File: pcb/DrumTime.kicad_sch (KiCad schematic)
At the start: 5 parts, among them U1 ESP32-S3-WROOM-1-N8

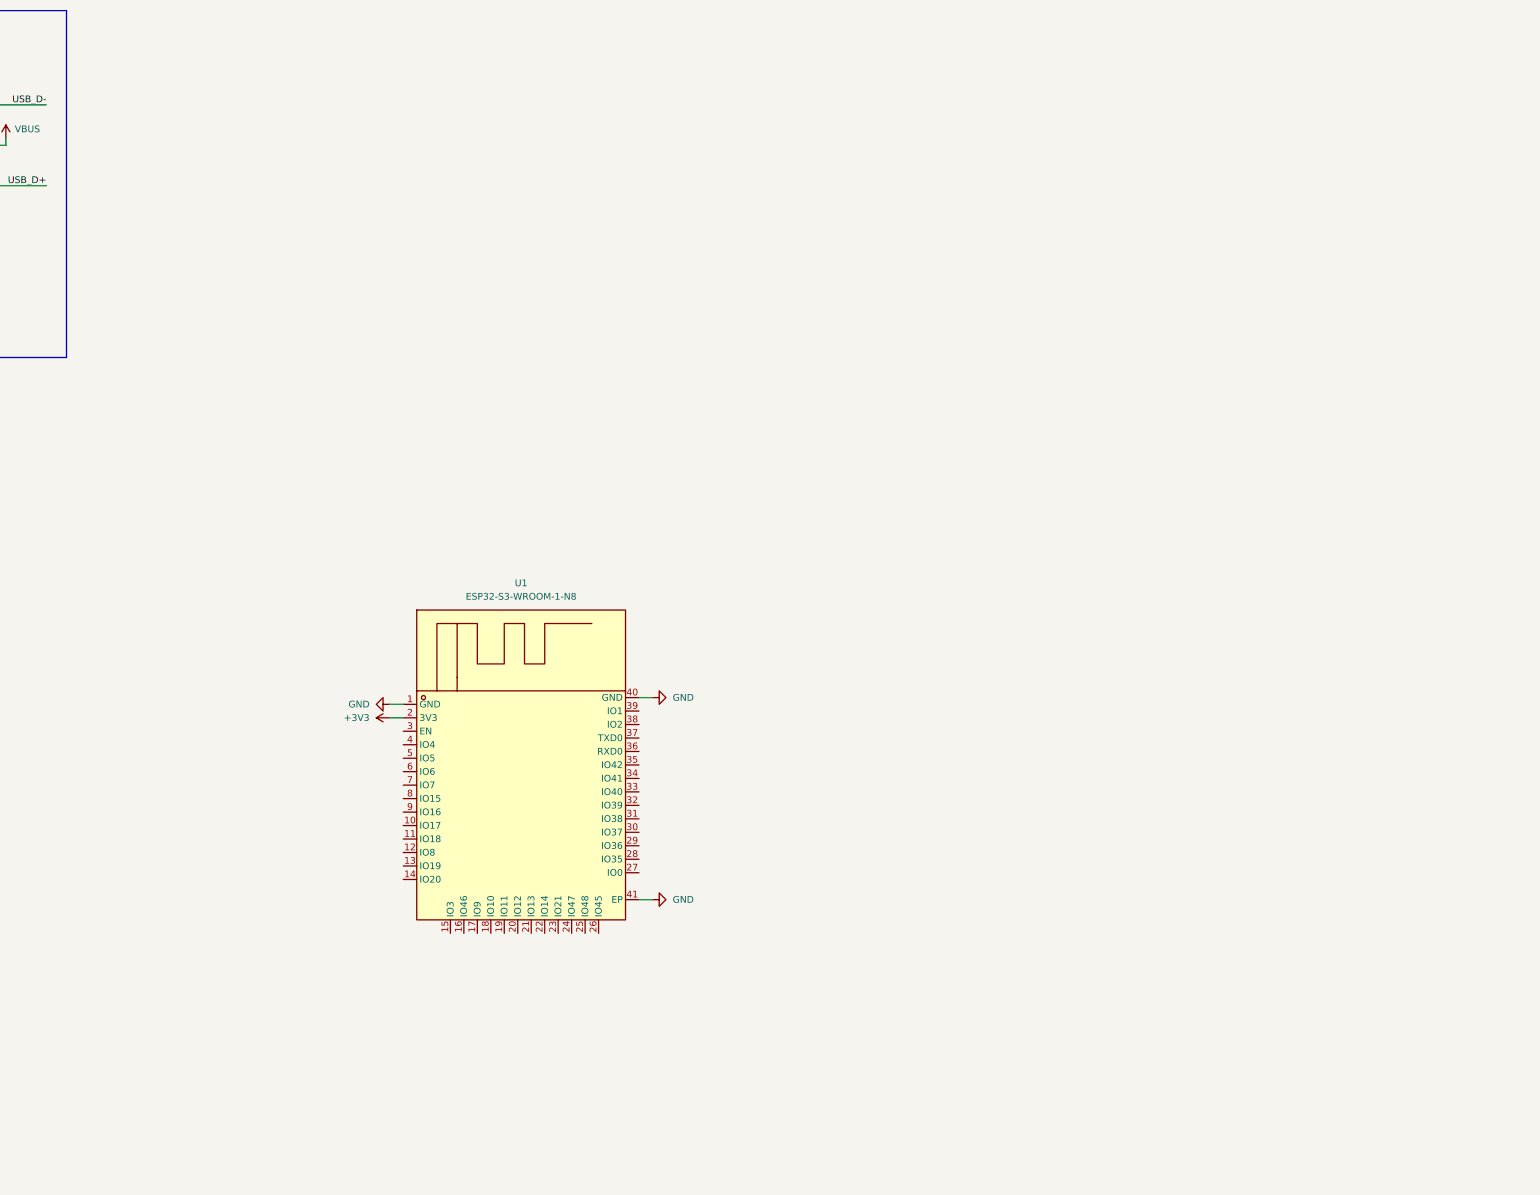
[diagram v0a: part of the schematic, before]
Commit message: feat(pcb/motors): add connections for the motors with hall effect sensors. (R_sense unspecified)
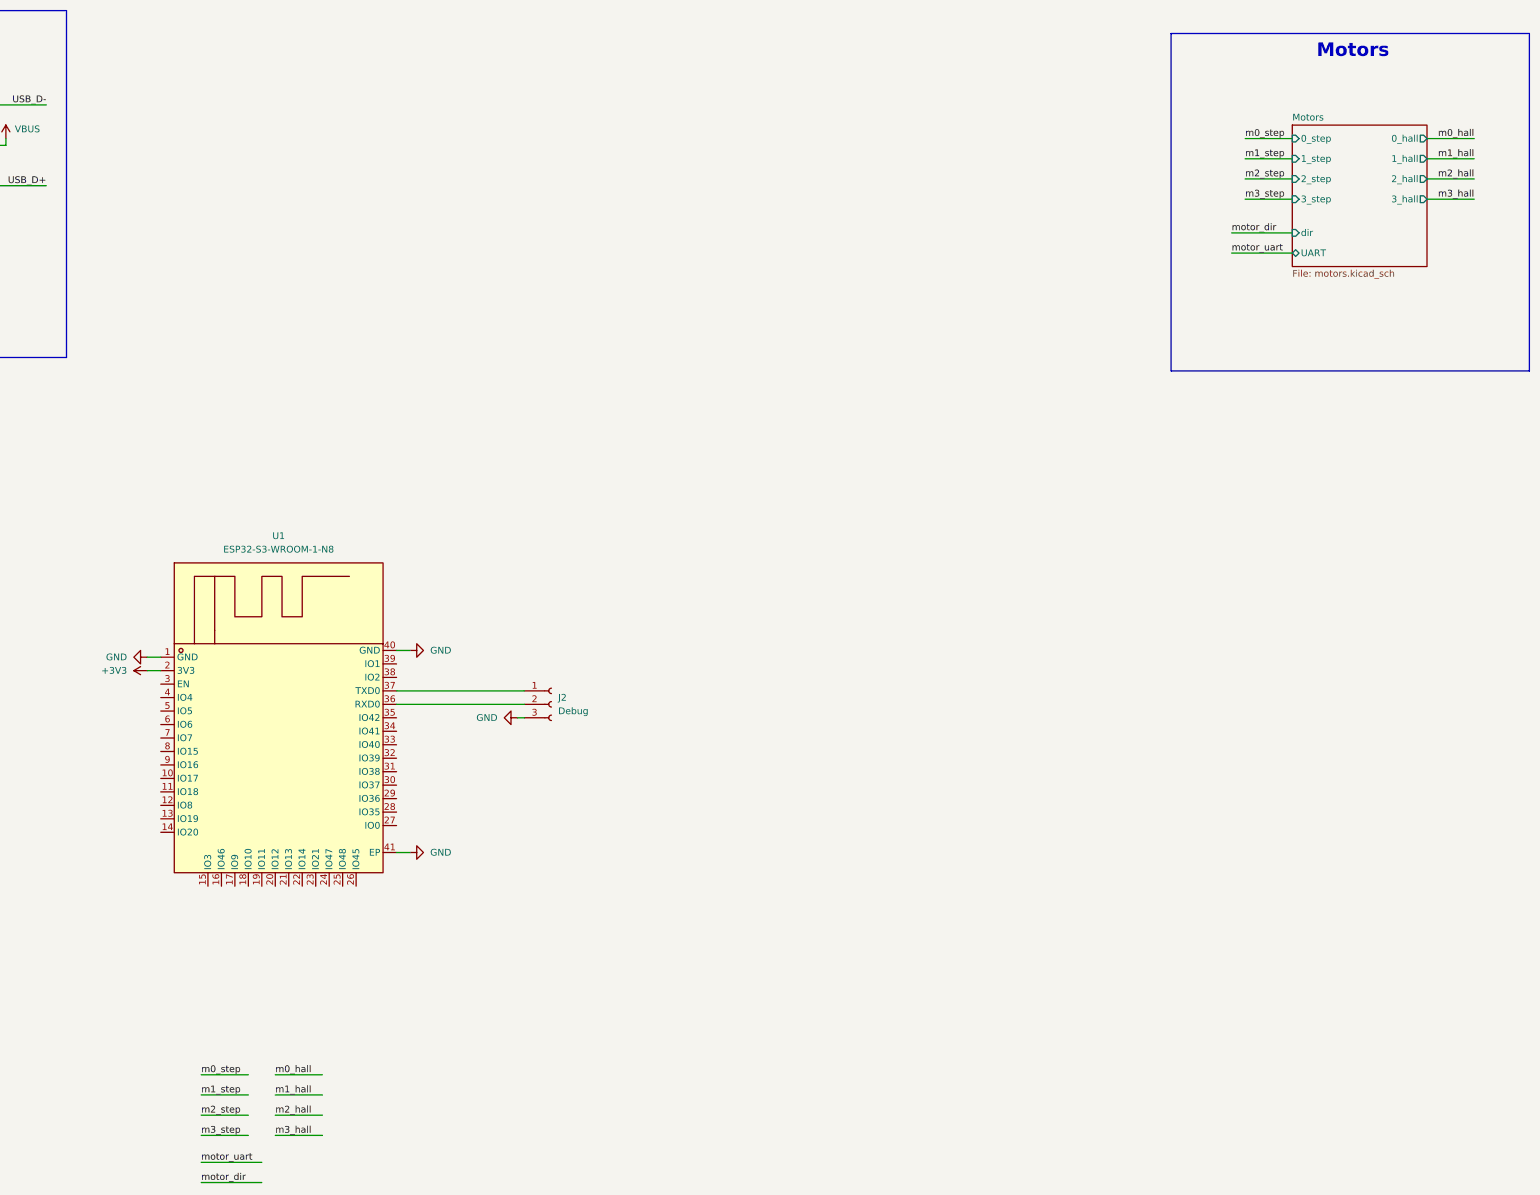
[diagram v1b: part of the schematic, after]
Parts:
- added J2: Debug, Connector_PinSocket_2.54mm:PinSocket_1x03_P2.54mm_Vertical, symbol Connector:Conn_01x03_Socket
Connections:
- net GND: now also J2.3 (Pin_3)
- net at U1.36 (RXD0): now also J2.2 (Pin_2)
- net at U1.37 (TXD0): now also J2.1 (Pin_1)
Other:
- added sheet Motors (motors.kicad_sch)
- note added: "Motors"
- moved on the sheet: U1

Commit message: feat(pcb/mcu): add ldo for 3v3 power and add needed passives and circuitry for MCU
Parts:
- added C29, C30, C31: 1uF, symbol Device:C
- added C32: 22uF, symbol Device:C
- added C33, C36: 100nF, symbol Device:C
- added C34, C35: C, symbol Device:C
- added J6: Boot, Jumper:SolderJumper-2_P1.3mm_Open_Pad1.0x1.5mm, symbol Connector:Conn_01x02_Socket
- added J7: EN, Jumper:SolderJumper-2_P1.3mm_Open_Pad1.0x1.5mm, symbol Connector:Conn_01x02_Socket
- added R15: 10kR, symbol Device:R
- added U8: TLV75533PDBVR, lcsc:SOT-23-5_L3.0-W1.7-P0.95-LS2.8-BR, symbol lcsc:TLV75533PDBVR
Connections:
- net +3V3: now also C29.1, C32.1, C33.1, R15.1, U8.5 (OUT)
- net GND: now also C29.2, C30.2, C31.2, C32.2, C33.2, C34.2, C35.2, C36.2, J6.2 (Pin_2), J7.2 (Pin_2), U8.2 (GND)
- net USB_D+: now also U1.14 (IO20), C35.1
- net USB_D-: now also U1.13 (IO19), C34.1
- net VBUS: now also C30.1, U8.1 (IN), U8.3 (EN)
- net m0_hall: now also U1.5 (IO5)
- net m0_step: now also U1.4 (IO4)
- net m1_hall: now also U1.7 (IO7)
- net m1_step: now also U1.6 (IO6)
- net m2_hall: now also U1.9 (IO16)
- net m2_step: now also U1.8 (IO15)
- net m3_hall: now also U1.11 (IO18)
- net m3_step: now also U1.10 (IO17)
- net motor_dir: now also U1.17 (IO9)
- net motor_uart: now also U1.12 (IO8)
- net at U1.27 (IO0): now also J6.1 (Pin_1)
- net at U1.3 (EN): now also C31.1, C36.1, J7.1 (Pin_1), R15.2
- no-connect marks 2 -> 6
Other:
- note added: "3V3 - LDO"
- note added: "JTAG"
- note added: "Seconds Indicator"
- note added: "Strapping JTAG"
- note added: "Strapping SPI"
- note added: "Strapping boot"
- moved on the sheet: J2, U1

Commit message: feat(pcb/leds): add seconds indicator light bar and misc rgb indicator
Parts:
- added C10: 1uF, symbol Device:C
- added C9: 100nF, symbol Device:C
- added LED1: SZYY1615RGB-A 4PIN, lcsc:LED-ARRAY-SMD_4P-L1.6-W1.5_SZYY1615RGB-A, symbol lcsc:SZYY1615RGB-A4PIN
- added R4, R6: 220R, lcsc:LED-ARRAY-SMD_4P-L1.6-W1.5_SZYY1615RGB-A, symbol Device:R
- added R5: 330R, lcsc:LED-ARRAY-SMD_4P-L1.6-W1.5_SZYY1615RGB-A, symbol Device:R
- added R7: R, symbol Device:R
- added U3, U4: TXS0108EPWR, lcsc:TSSOP-20_L6.5-W4.4-P0.65-LS6.4-BL, symbol lcsc:TXS0108EPWR
- added U5: IS31FL3236A-QFLS2-TR, lcsc:QFN-44_L5.0-W5.0-P0.40-BL-EP, symbol lcsc:IS31FL3236A-QFLS2-TR
- renumbered C30 to C1, C29 to C2, C32 to C3, C36 to C4, C33 to C5, C34 to C6, C31 to C7, C35 to C8, J7 to J1, J6 to J3, R15 to R3, U8 to U1, U1 to U2
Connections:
- net +3V3: now also U3.10 (OE), U3.2 (VCCA), U4.10 (OE), U4.2 (VCCA)
- net GND: now also C10.2, C9.2, LED1.4 (K), R7.2, U3.11 (GND), U4.11 (GND), U5.17 (GND), U5.37 (AD), U5.39 (GND), U5.45 (EPAD)
- net m0_hall: now also U3.5 (A4)
- net m0_step: now also U3.4 (A3)
- net m1_hall: now also U3.7 (A6)
- net m1_step: now also U3.6 (A5)
- net m2_hall: now also U3.9 (A8)
- net m2_step: now also U3.8 (A7)
- net m3_hall: now also U4.3 (A2)
- net m3_step: now also U4.1 (A1)
- net motor_dir: now also U3.3 (A2)
- net motor_uart: now also U3.1 (A1), U3.20 (B1)
- net at C4.1, J1.1 (Pin_1), U2.3 (EN): no longer C7.1, R3.2
- net SCL: now reaches U2.18 (IO10)
- net SCL: now also U4.4 (A3)
- net SDA: now reaches U2.19 (IO11)
- net SDA: now also U4.5 (A4)
- net RGB_B: now reaches U2.29 (IO36)
- net RGB_B: now also R6.1
- net RGB_G: now reaches U2.30 (IO37)
- net RGB_G: now also R4.1
- net RGB_R: now reaches U2.31 (IO38)
- net RGB_R: now also R5.2
- net VBUS renamed +5V
- net +5V: now also C10.1, C9.1, U3.19 (VCCB), U4.19 (VCCB), U5.36 (SDB), U5.38 (VCC)
- new net: C7.1, R3.2
- new net: LED1.3 (A), R6.2
- new net: R7.1, U5.40 (R-EXT)
- new net: LED1.2 (A), R4.2
- new net: LED1.1 (A), R5.1
- new net 5V_SCL: U4.17 (B3), U5.42 (SCL)
- new net 5V_SDA: U4.16 (B4), U5.41 (SDA)
- new net LEDs/1: U5.43 (OUT1)
- new net LEDs/10: U5.8 (OUT10)
- new net LEDs/11: U5.9 (OUT11)
- new net LEDs/12: U5.10 (OUT12)
- new net LEDs/13: U5.11 (OUT13)
- new net LEDs/14: U5.12 (OUT14)
- new net LEDs/15: U5.13 (OUT15)
- new net LEDs/16: U5.14 (OUT16)
- new net LEDs/17: U5.15 (OUT17)
- new net LEDs/18: U5.16 (OUT18)
- new net LEDs/19: U5.18 (OUT19)
- new net LEDs/2: U5.44 (OUT2)
- new net LEDs/20: U5.19 (OUT20)
- new net LEDs/21: U5.20 (OUT21)
- new net LEDs/22: U5.21 (OUT22)
- new net LEDs/23: U5.22 (OUT23)
- new net LEDs/24: U5.23 (OUT24)
- new net LEDs/25: U5.24 (OUT25)
- new net LEDs/26: U5.25 (OUT26)
- new net LEDs/27: U5.26 (OUT27)
- new net LEDs/28: U5.27 (OUT28)
- new net LEDs/29: U5.28 (OUT29)
- new net LEDs/3: U5.1 (OUT3)
- new net LEDs/30: U5.29 (OUT30)
- new net LEDs/31: U5.30 (OUT31)
- new net LEDs/32: U5.31 (OUT32)
- new net LEDs/33: U5.32 (OUT33)
- new net LEDs/34: U5.33 (OUT34)
- new net LEDs/35: U5.34 (OUT35)
- new net LEDs/36: U5.35 (OUT36)
- new net LEDs/4: U5.2 (OUT4)
- new net LEDs/5: U5.3 (OUT5)
- new net LEDs/6: U5.4 (OUT6)
- new net LEDs/7: U5.5 (OUT7)
- new net LEDs/8: U5.6 (OUT8)
- new net LEDs/9: U5.7 (OUT9)
- new net motor_hall_0: U3.16 (B4)
- new net motor_hall_1: U3.14 (B6)
- new net motor_hall_2: U3.12 (B8)
- new net motor_hall_3: U4.18 (B2)
- new net motor_step_0: U3.17 (B3)
- new net motor_step_1: U3.15 (B5)
- new net motor_step_2: U3.13 (B7)
- new net motor_step_3: U4.20 (B1)
- new net motors_dir: U3.18 (B2)
- no-connect marks 6 -> 27
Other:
- removed sheet Motors
- added sheet LEDs (leds.kicad_sch)
- added sheet Motor (motor.kicad_sch)
- added sheet Motor1 (motor.kicad_sch)
- added sheet Motor2 (motor.kicad_sch)
- added sheet Motor3 (motor.kicad_sch)
- note added: "5V-3V3 Level shifters"
- note added: "Misc. Indicator"
- moved on the sheet: C3, C4, C5, C6, C7, C8, J1, J2, J3, R3, U2

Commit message: feat(pcb/leds): add LDR
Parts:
- added R20: GL5528, lcsc:RES-TH_L5.1-W4.3-P3.40-D0.5, symbol lcsc:GL5528
- added R21: R, symbol Device:R
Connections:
- net +3V3: now also R21.2
- net GND: now also R20.2
- net LDR_sense: now reaches U2.39 (IO1)
- net LDR_sense: now also R20.1, R21.1
- no-connect marks 27 -> 26
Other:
- note added: "LDR"
- note added: "TODO: add value to LDR voltage divider resistor"
- note added: "TODO: set R_ext for setting LED current"

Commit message: feat(pcb): remove levelshifters, change to 3v3 vcc_io on tmc2209s, add rgb led to led driver, add R_ext value for led driver, add R_sense value for tmc2209s, add seperate dir signals for each tmc2209
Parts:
- removed LED1: SZYY1615RGB-A 4PIN, lcsc:LED-ARRAY-SMD_4P-L1.6-W1.5_SZYY1615RGB-A, symbol lcsc:SZYY1615RGB-A4PIN
- removed R4: 220R, lcsc:LED-ARRAY-SMD_4P-L1.6-W1.5_SZYY1615RGB-A, symbol Device:R
- removed R5: 330R, lcsc:LED-ARRAY-SMD_4P-L1.6-W1.5_SZYY1615RGB-A, symbol Device:R
- removed U3, U4: TXS0108EPWR, lcsc:TSSOP-20_L6.5-W4.4-P0.65-LS6.4-BL, symbol lcsc:TXS0108EPWR
- added C2: 100nF, symbol Device:C
- added D2: BAT60B, lcsc:SOD-323_L1.7-W1.3-LS2.6-RD-1, symbol lcsc:BAT60B_C7502695
- added R7: 4.7kR, symbol Device:R
- added R8: 4.7kR, lcsc:LED-ARRAY-SMD_4P-L1.6-W0.8-BL-FD, symbol Device:R
- added U3: TJ-S1608SW6TDSLCCYRGB-A5, lcsc:LED-ARRAY-SMD_4P-L1.6-W0.8-BL-FD, symbol lcsc:TJ-S1608SW6TDSLCCYRGB-A5
- R1: renamed from R21; value R -> 10kR
- R6: value 220R -> 4.7kR; footprint lcsc:LED-ARRAY-SMD_4P-L1.6-W1.5_SZYY1615RGB-A -> (none)
- R9: renamed from R7; value R -> 15kR
- renumbered C9 to C10, C10 to C11, C2 to C3, C3 to C4, C4 to C5, C5 to C6, C6 to C7, C7 to C8, C8 to C9, R20 to R2, R1 to R3, R2 to R4, R3 to R5, U5 to U4
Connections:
- net 5V_SCL is gone; now on net SCL: U4.42 (SCL)
- net 5V_SDA is gone; now on net SDA: U4.41 (SDA)
- net LEDs/34 is gone; now on net RGB_R: U4.33 (OUT34)
- net LEDs/35 is gone; now on net RGB_G: U4.34 (OUT35)
- net LEDs/36 is gone; now on net RGB_B: U4.35 (OUT36)
- net motor_dir is gone; now on net m2_hall: U2.17 (IO9)
- net motor_uart is gone; now on net m2_step: U2.12 (IO8)
- net +3V3: now also R6.1, R7.1, R8.1
- net +5V: now also U3.1 (+)
- net GND: now also C2.2
- net LDR_sense: now also C2.1
- net RGB_B: now also U3.2 (-); no longer R6.1, U2.29 (IO36)
- net RGB_G: now also U3.3 (-); no longer U2.30 (IO37)
- net RGB_R: now also U3.4 (-); no longer U2.31 (IO38)
- net SCL: now also U2.22 (IO14), R7.2; no longer U2.18 (IO10)
- net SDA: now also R6.2, U2.23 (IO21); no longer U2.19 (IO11)
- net m1_hall: now also U2.8 (IO15); no longer U2.7 (IO7)
- net m1_step: now also U2.7 (IO7); no longer U2.6 (IO6)
- net m2_hall: no longer U2.9 (IO16)
- net m2_step: no longer U2.8 (IO15)
- net m3_hall: now also U2.20 (IO12); no longer U2.11 (IO18)
- net m3_step: now also U2.19 (IO11); no longer U2.10 (IO17)
- net m3_dir: now reaches U2.21 (IO13)
- new net m0_dir: U2.6 (IO6)
- new net m1_dir: U2.9 (IO16)
- new net m2_dir: U2.18 (IO10)
- new net m_uart: D2.2 (A), R8.2, U2.11 (IO18)
- new net uart1_tx: D2.1 (K), U2.10 (IO17)
- no-connect marks 26 -> 17
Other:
- sheet LEDs ports: added none; removed 34, 35, 36
- note added: "Results in I_max = 5.07mA"
- note removed: "5V-3V3 Level shifters"
- note removed: "TODO: add value to LDR voltage divider resistor"
- note removed: "TODO: set R_ext for setting LED current"
- moved on the sheet: C4, C5, C6, C7, C8, C9, J1, J2, J3, R1, R2, R5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

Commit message: feat(pcb): add a central ENN connection to all motor drivers, switch LDO to one with higher input voltage tolerances and add PTC fuse
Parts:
- removed U1: TLV75533PDBVR, lcsc:SOT-23-5_L3.0-W1.7-P0.95-LS2.8-BR, symbol lcsc:TLV75533PDBVR
- added F2: Polyfuse, lcsc:F2920, symbol Device:Polyfuse
- added JP1: JMP Fuse, Jumper:SolderJumper-2_P1.3mm_Open_TrianglePad1.0x1.5mm, symbol Jumper:SolderJumper_2_Open
- added R22: 10kR, symbol Device:R
- added U1: ME6210A33PG, lcsc:SOT-89_L4.5-W2.5-P1.50-LS4.2-BR, symbol lcsc:ME6210A33PG
- C1, C3: value 1uF -> 10uF
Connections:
- net +3V3: now also R22.1, U1.3 (Vout)
- net +5V: now also F2.2, JP1.2 (B), U1.2 (Vin); no longer D1.5, USB1.A4 (VBUS), USB1.A9 (VBUS), USB1.B4 (VBUS), USB1.B9 (VBUS)
- net GND: now also U1.1 (Vss)
- net SCL: now also U2.23 (IO21); no longer U2.22 (IO14)
- net SDA: now also U2.24 (IO47); no longer U2.23 (IO21)
- new net VBUS: D1.5, F2.1, JP1.1 (A), USB1.A4 (VBUS), USB1.A9 (VBUS), USB1.B4 (VBUS), USB1.B9 (VBUS)
- new net m_enn: R22.2, U2.22 (IO14)
- no-connect marks 17 -> 15
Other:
- sheet Motor ports: added ENN; removed none
- sheet Motor1 ports: added ENN; removed none
- sheet Motor2 ports: added ENN; removed none
- sheet Motor3 ports: added ENN; removed none
- note added: "Fuse"
- moved on the sheet: C1, C10, C11, C2, C3, R1, R2, R9, U4

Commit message: feat(pcb): source all parts, switch to straight tht usb to mount on back and add series resistor LED driver to prevent over voltage
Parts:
- removed USB1: USB4145-03-0070-C, lcsc:USB-C-SMD_USB4145-03-0070-C, symbol lcsc:USB4145-03-0070-C
- added C3: 100uF, lcsc:CAP-SMD_BD6.3-L6.6-W6.6-FD, symbol Device:C_Polarized
- added J4, J5: LED_Conn, Connector_PinHeader_2.54mm:PinHeader_1x04_P2.54mm_Vertical, symbol Connector_Generic:Conn_01x04
- added R27: 10R, Resistor_SMD:R_0805_2012Metric, symbol Device:R
- added USB1: Type-C, lcsc:USB-C-TH_TYPE-C16PLCH10.0-B143, symbol lcsc:HX-TYPE-C16P180LC-BH13.0
- C1: footprint (none) -> Capacitor_SMD:C_0805_2012Metric; LCSC Part (none) -> C15850
- C11: renamed from C10; footprint (none) -> Capacitor_SMD:C_0603_1608Metric; LCSC Part (none) -> C14663
- C12: renamed from C11; footprint (none) -> Capacitor_SMD:C_0603_1608Metric; LCSC Part (none) -> C15849
- C2: footprint (none) -> Capacitor_SMD:C_0603_1608Metric; LCSC Part (none) -> C14663
- C4: renamed from C3; footprint (none) -> Capacitor_SMD:C_0805_2012Metric; LCSC Part (none) -> C15850
- C5: renamed from C4; footprint (none) -> Capacitor_SMD:C_0805_2012Metric; LCSC Part (none) -> C45783
- C6: renamed from C5; footprint (none) -> Capacitor_SMD:C_0603_1608Metric; LCSC Part (none) -> C14663
- C7: renamed from C6; footprint (none) -> Capacitor_SMD:C_0603_1608Metric; LCSC Part (none) -> C14663
- C9: renamed from C8; footprint (none) -> Capacitor_SMD:C_0603_1608Metric; LCSC Part (none) -> C15849
- J1, J2, J3: now left out of the parts list
- R1, R5: footprint (none) -> Resistor_SMD:R_0603_1608Metric; LCSC Part (none) -> C25804
- R10: renamed from R9; footprint (none) -> Resistor_SMD:R_0603_1608Metric; LCSC Part (none) -> C2906995
- R3, R4: LCSC Part (none) -> C23186
- R6, R7: value 4.7kR -> 5.1kR; footprint (none) -> Resistor_SMD:R_0603_1608Metric; LCSC Part (none) -> C23186
- R8: value 4.7kR -> 5.1kR; footprint lcsc:LED-ARRAY-SMD_4P-L1.6-W0.8-BL-FD -> Resistor_SMD:R_0603_1608Metric; LCSC Part (none) -> C23186
- R9: renamed from R22; footprint (none) -> Resistor_SMD:R_0603_1608Metric; LCSC Part (none) -> C25804
- renumbered C9 to C10, C7 to C8, F2 to F1
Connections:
- net +5V: now also C3.1, J4.1 (Pin_1), J5.1 (Pin_1), R27.1; no longer C11.1, C12.1, U4.38 (VCC)
- net GND: now also C3.2, J4.4 (Pin_4), J5.4 (Pin_4), USB1.0 (EH), USB1.A1 (GND), USB1.A12 (GND), USB1.B1 (GND), USB1.B12 (GND)
- net SCL: now also J4.2 (Pin_2), J5.2 (Pin_2)
- net SDA: now also J4.3 (Pin_3), J5.3 (Pin_3)
- net USB_D+: now also USB1.A6 (DP1), USB1.B6 (DP2)
- net USB_D-: now also USB1.A7 (DN1), USB1.B7 (DN2)
- net VBUS: now also USB1.A4 (VBUS), USB1.A9 (VBUS), USB1.B4 (VBUS), USB1.B9 (VBUS)
- net cc1: now also USB1.A5 (CC1)
- net cc2: now also USB1.B5 (CC2)
- new net: C11.1, C12.1, R27.2, U4.38 (VCC)
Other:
- moved on the sheet: C11, C12, D1, F1, JP1, R10, R3, R4, U4

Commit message: feat(pcb): layout and route LED section
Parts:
- removed J2: Debug, Connector_PinSocket_2.54mm:PinSocket_1x03_P2.54mm_Vertical, symbol Connector:Conn_01x03_Socket
- added FID1: Fiducial, Fiducial:Fiducial_Cross_1.5mm_Mask2mm, symbol Mechanical:Fiducial
- added FID2: Fiducial, Fiducial:Fiducial_0.75mm_Mask1.5mm, symbol Mechanical:Fiducial
- added H1, H2, H3, H4, H5, H6: MountingHole, MountingHole:MountingHole_2.2mm_M2_Pad, symbol Mechanical:MountingHole_Pad
- added J3: Debug, Connector_PinSocket_2.54mm:PinSocket_1x03_P2.54mm_Vertical, symbol Connector:Conn_01x03_Socket
- renumbered J3 to J2, R9 to R10, R10 to R11, R27 to R9
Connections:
- net GND: now also H1.1, H2.1, H3.1, H4.1, H5.1, H6.1, J3.1 (Pin_1)
- net SCL: now also J4.3 (Pin_3), J5.3 (Pin_3); no longer J4.2 (Pin_2), J5.2 (Pin_2)
- net SDA: now also J4.2 (Pin_2), J5.2 (Pin_2); no longer J4.3 (Pin_3), J5.3 (Pin_3)
- net at C9.1, R5.2: now also C6.1, J1.1 (Pin_1), U2.3 (EN)
- net at U2.36 (RXD0): now also J3.3 (Pin_3)
- net at U2.37 (TXD0): now also J3.2 (Pin_2)
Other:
- note added: "LED"
- note added: "Mounting"
